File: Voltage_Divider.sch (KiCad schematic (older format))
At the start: 36 parts, among them J24 test, J25 CONN_01X05, J26 test, J27 test, U19 ACPL-W343, U20 ACPL-W343, U21 ANA4522

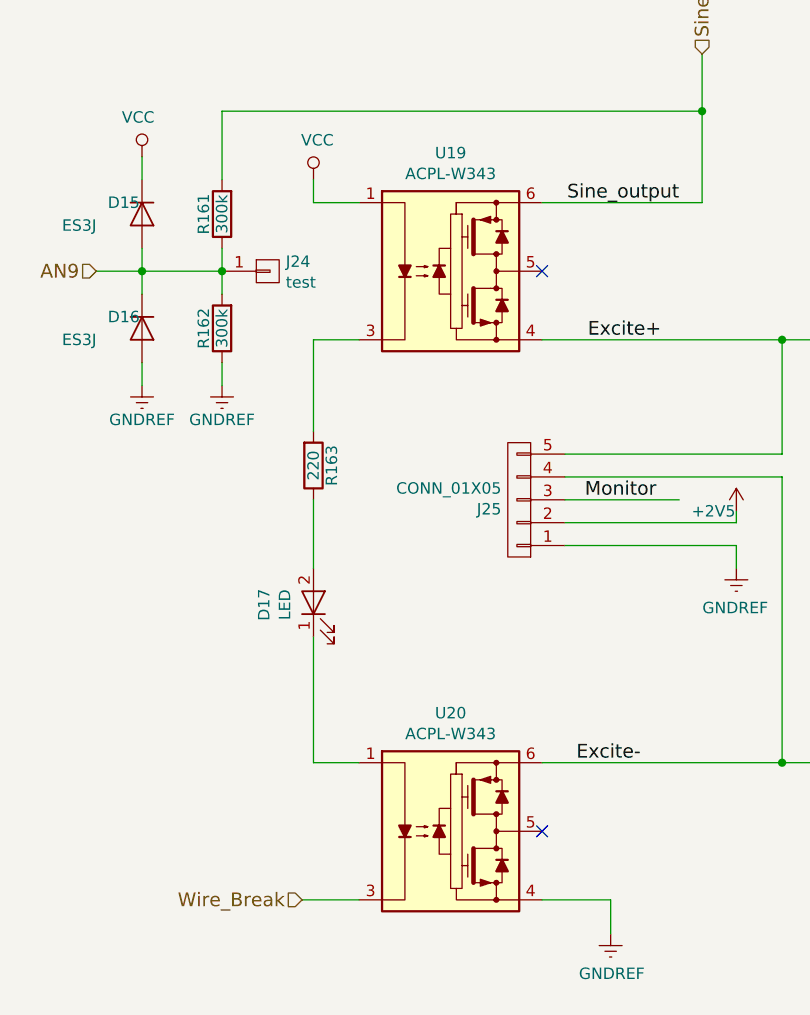
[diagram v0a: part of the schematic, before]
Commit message: 2차 PCB 1차 수정
1. ADR455 Vcc V12 수정
2. DCDC 입력전압 변경
3. Bypass 콘덴서 C66, C67 추가
4. SOIC 방향 표시
5. TLV431 PADS 변경
6. AQV258 Pin3 --> Pin2
7. 전해콘덴서 방향추가
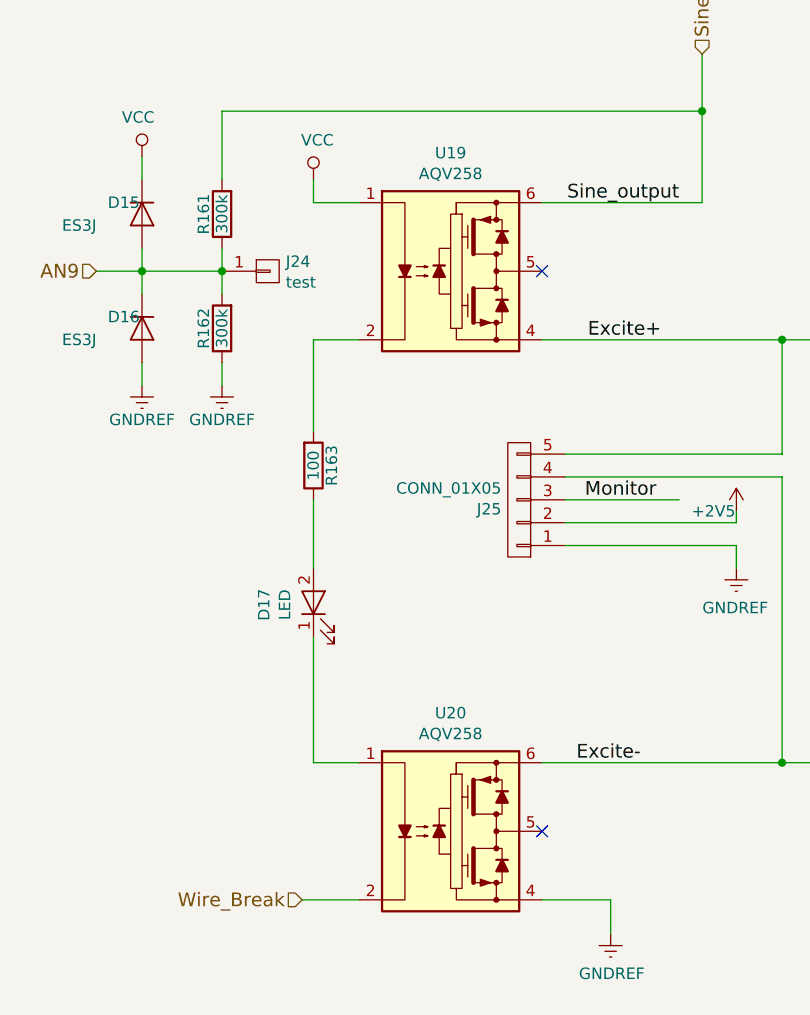
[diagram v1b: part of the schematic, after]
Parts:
- removed U19, U20: ACPL-W343, Housings_DIP:DIP-6_W7.62mm, symbol ACPL-W343
- added U19, U20: AQV258, Housings_DIP:DIP-6_W7.62mm_Socket, symbol AQV258
- R163: value 220 -> 100
- U21: footprint Housings_SOIC:SOIC-8-1EP_3.9x4.9mm_Pitch1.27mm -> USER:SOIC-8_3.9x4.9mm_Pitch1.27mm
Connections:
- net Excite+: now also U19.4 (VEE)
- net Excite-: now also U20.6 (VCC)
- net GNDREF: now also U20.4 (VEE)
- net Sine: now also U19.6 (VCC)
- net VCC: now also U19.1 (A)
- net Wire_Break: now also U20.2 (C)
- net at R163.2: now also U19.2 (C)
- net at D17.1 (K): now also U20.1 (A)
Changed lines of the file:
@@
 F 0 "U21" H 9891 2996 50  0000 L CNN
 F 1 "ANA4522" H 9891 2905 50  0000 L CNN
-F 2 "Housings_SOIC:SOIC-8-1EP_3.9x4.9mm_Pitch1.27mm" H 9550 2950 50  0001 C CNN
+F 2 "USER:SOIC-8_3.9x4.9mm_Pitch1.27mm" H 9550 2950 50  0001 C CNN
 F 3 "" H 9550 2950 50  0001 C CNN
 	1    9550 2950
@@
 P 3500 3400
 F 0 "R163" V 3580 3400 50  0000 C CNN
-F 1 "220" V 3500 3400 50  0000 C CNN
+F 1 "100" V 3500 3400 50  0000 C CNN
 F 2 "Resistors_SMD:R_0805_HandSoldering" V 3430 3400 50  0001 C CNN
 F 3 "" H 3500 3400 50  0001 C CNN
@@
 Text Label 5100 2250 2    60   ~ 0
 Sine_output
-$Comp
-L ACPL-W343 U20
-U 1 1 5B064611
-P 4100 5000
-F 0 "U20" H 4100 5517 50  0000 C CNN
-F 1 "ACPL-W343" H 4100 5426 50  0000 C CNN
-F 2 "Housings_DIP:DIP-6_W7.62mm" H 4100 4600 50  0001 C CIN
-F 3 "" H 4010 5005 50  0001 L CNN
-	1    4100 5000
-	1    0    0    -1
-$EndComp
 NoConn ~ 4500 5000
-$Comp
-L ACPL-W343 U19
-U 1 1 5B06461B
-P 4100 2550
-F 0 "U19" H 4100 3067 50  0000 C CNN
-F 1 "ACPL-W343" H 4100 2976 50  0000 C CNN
-F 2 "Housings_DIP:DIP-6_W7.62mm" H 4100 2150 50  0001 C CIN
-F 3 "" H 4010 2555 50  0001 L CNN
-	1    4100 2550
-	1    0    0    -1
-$EndComp
 $Comp
 L 1N4004 D16
@@
 Wire Wire Line
 	4500 2850 8000 2850
+$Comp
+L AQV258 U19
+U 1 1 5B1E85BB
+P 4100 2550
+F 0 "U19" H 4100 3067 50  0000 C CNN
+F 1 "AQV258" H 4100 2976 50  0000 C CNN
+F 2 "Housings_DIP:DIP-6_W7.62mm_Socket" H 4100 2150 50  0001 C CIN
+F 3 "" H 4010 2555 50  0001 L CNN
+	1    4100 2550
+	1    0    0    -1
+$EndComp
+$Comp
+L AQV258 U20
+U 1 1 5B1E8691
+P 4100 5000
+F 0 "U20" H 4100 5517 50  0000 C CNN
+F 1 "AQV258" H 4100 5426 50  0000 C CNN
+F 2 "Housings_DIP:DIP-6_W7.62mm_Socket" H 4100 4600 50  0001 C CIN
+F 3 "" H 4010 5005 50  0001 L CNN
+	1    4100 5000
+	1    0    0    -1
+$EndComp
 $EndSCHEMATC

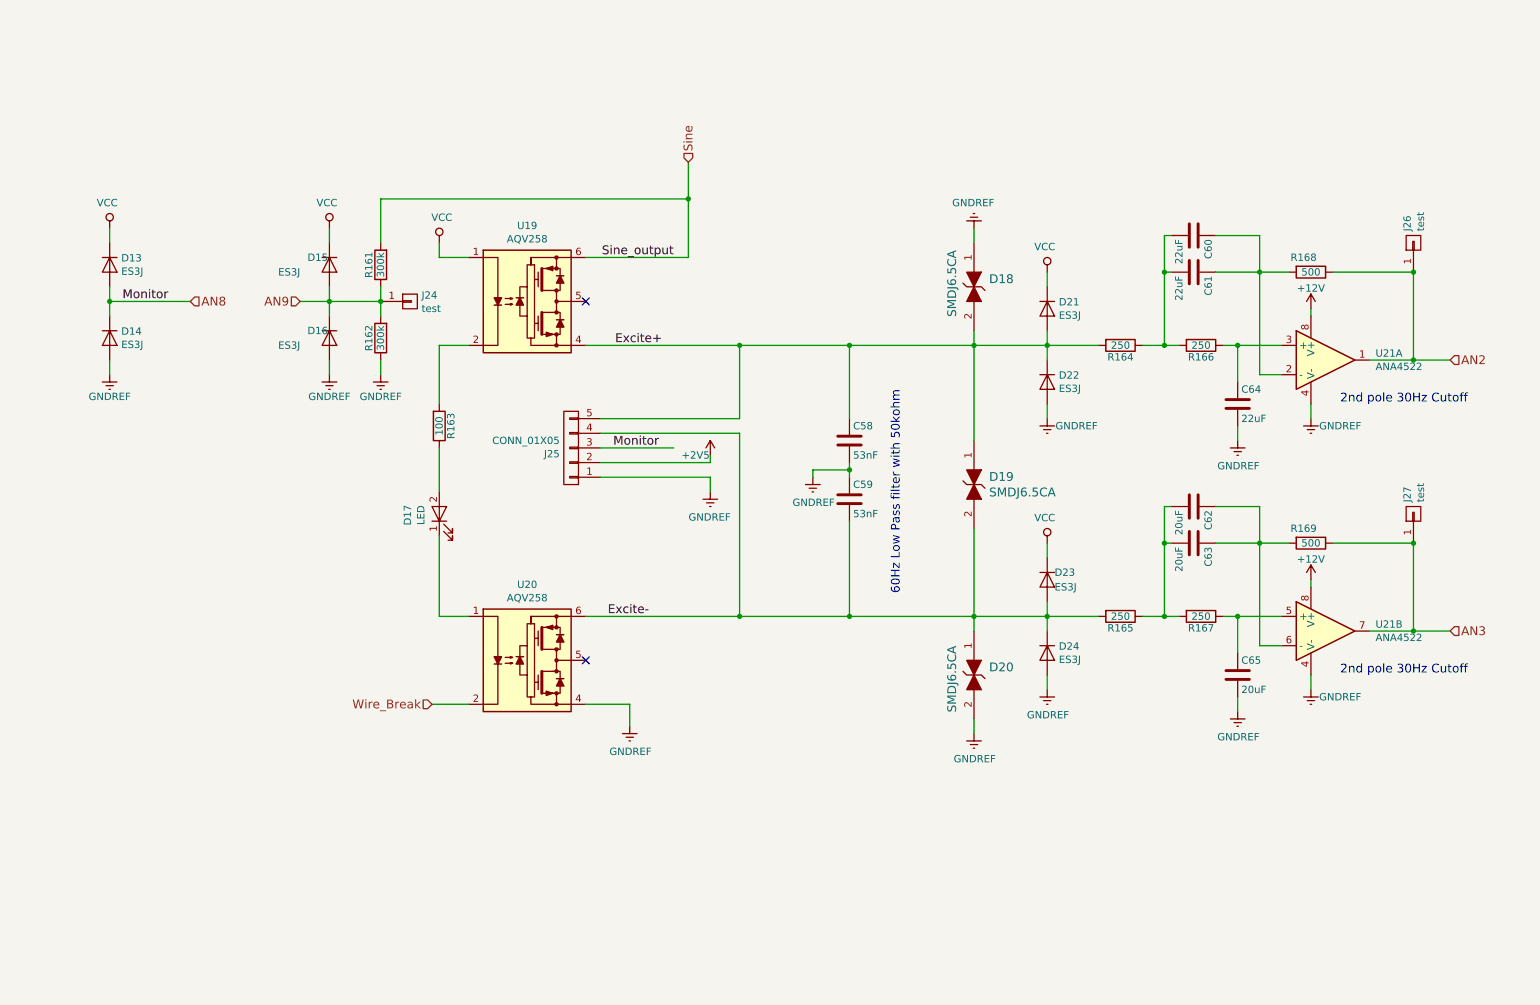
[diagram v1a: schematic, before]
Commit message: 0805_넓히기
기타 수정
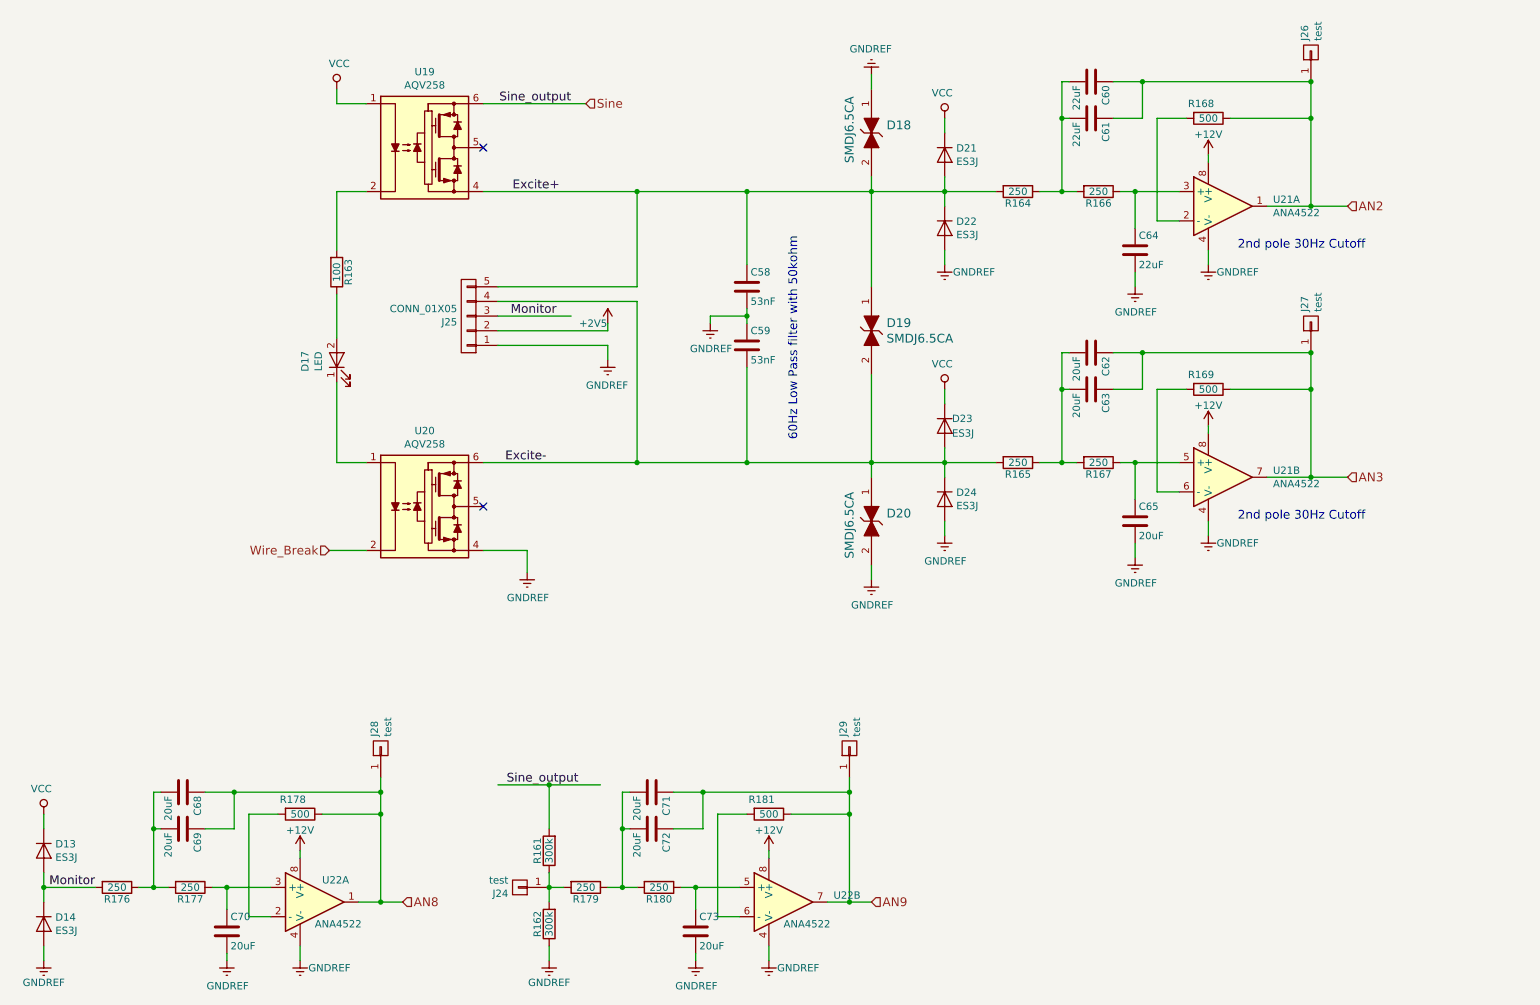
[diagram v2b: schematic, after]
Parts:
- removed D15, D16: ES3J, Diodes_SMD:D_SMC_Handsoldering, symbol 1N4004
- added C68, C69, C70, C71, C72, C73: 20uF, Capacitors_SMD:C_1210_HandSoldering, symbol C
- added J28, J29: test, Pin_Headers:Pin_Header_Straight_1x01_Pitch2.00mm, symbol CONN_01X01
- added R176, R177, R179, R180: 250, Resistors_SMD:R_0805_HandSoldering, symbol R
- added R178, R181: 500, Resistors_SMD:R_0805_HandSoldering, symbol R
- added U22: ANA4522, USER:SOIC-8_3.9x4.9mm_Pitch1.27mm, symbol LM358
- D13, D14, D21, D22, D23, D24: footprint Diodes_SMD:D_SMC_Handsoldering -> USER:D_SMC_Handsoldering
- U21: footprint Housings_SOIC:SOIC-8-1EP_3.9x4.9mm_Pitch1.27mm -> USER:SOIC-8_3.9x4.9mm_Pitch1.27mm
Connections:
- net +12V: now also U22.8 (V+), U22.8 (V+)
- net AN2: now also C60.1, C61.1
- net AN3: now also C62.1, C63.1
- net AN8: now also C68.1, C69.1, J28.1 (P1), R178.1, U22.1; no longer D13.2 (A), D14.1 (K), J25.3 (P3)
- net AN9: now also C71.1, C72.1, J29.1 (P1), R181.1, U22.7; no longer J24.1 (P1), R161.1, R162.2
- net GNDREF: now also C70.2, C73.2, U22.4 (V-), U22.4 (V-)
- net at R168.2, U21.2 (-): no longer C60.1, C61.1
- net at R169.2, U21.6 (-): no longer C62.1, C63.1
- new net: J24.1 (P1), R161.1, R162.2, R179.2
- new net: R178.2, U22.2 (-)
- new net: C70.1, R177.1, U22.3 (+)
- new net: C68.2, C69.2, R176.1, R177.2
- new net: C71.2, C72.2, R179.1, R180.2
- new net: C73.1, R180.1, U22.5 (+)
- new net: R181.2, U22.6 (-)
- new net Monitor: D13.2 (A), D14.1 (K), J25.3 (P3), R176.2
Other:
- moved on the sheet: C58, C59, C60, C61, C62, C63, C64, C65, D13, D14, D17, D18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

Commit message: High Voltage reinforce
고전압 부분 보강
AN2, AN3 두 부분 6.5V limit
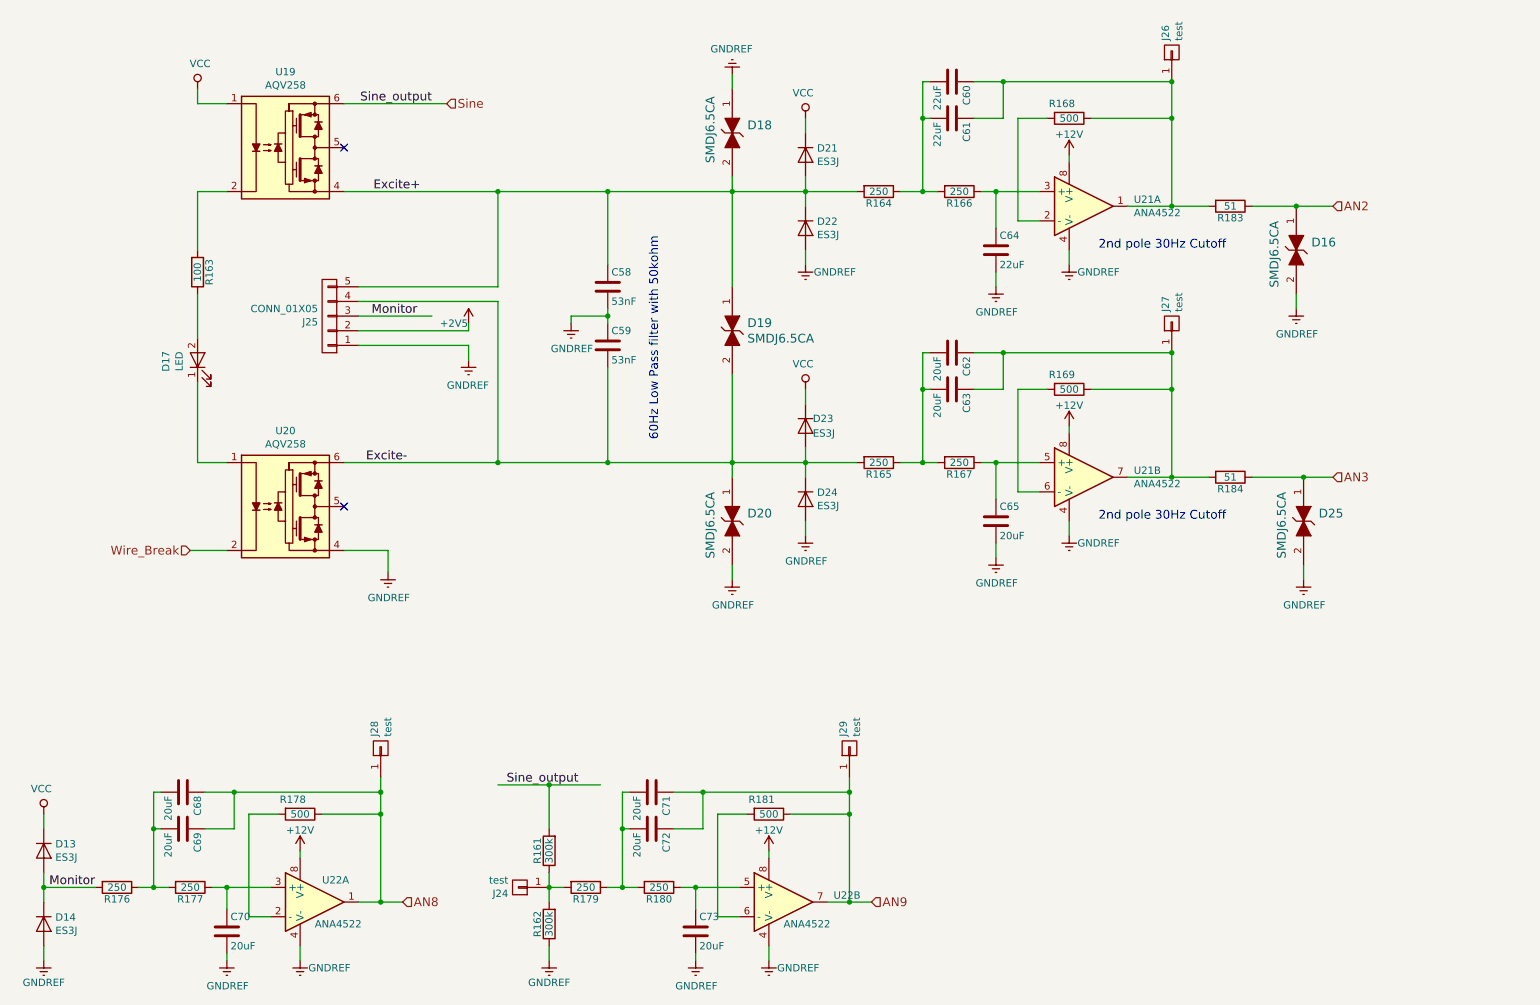
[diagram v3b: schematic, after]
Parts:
- added D16, D25: SMDJ6.5CA, Diodes_SMD:D_SMC_Handsoldering, symbol PGB1010603MR
- added R183, R184: 51, Resistors_SMD:R_0805_HandSoldering, symbol R
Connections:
- net AN2: now also D16.1, R183.1; no longer C60.1, C61.1, J26.1 (P1), R168.1, U21.1
- net AN3: now also D25.1, R184.1; no longer C62.1, C63.1, J27.1 (P1), R169.1, U21.7
- net GNDREF: now also D16.2, D25.2
- new net: C60.1, C61.1, J26.1 (P1), R168.1, R183.2, U21.1
- new net: C62.1, C63.1, J27.1 (P1), R169.1, R184.2, U21.7
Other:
- moved on the sheet: C58, C59, C60, C61, C62, C63, C64, C65, D17, D18, D19, D20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

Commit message: 3차 PCB
1. 모니터 고압부 150k옴 2갤로 수정
2. 6.5V Zener 추가
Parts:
- D18, D19, D20: value SMDJ6.5CA -> SMDJ10
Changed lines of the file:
@@
 P 5500 1400
 F 0 "D18" V 5447 1503 60  0000 L CNN
-F 1 "SMDJ6.5CA" H 5250 1250 60  0000 L CNN
+F 1 "SMDJ10" H 5250 1250 60  0000 L CNN
 F 2 "Diodes_SMD:D_SMC_Handsoldering" H 5700 1600 60  0001 L CNN
 F 3 "http://www.littelfuse.com/data/en/data_sheets/littelfuse_pulseguard-esd_pgb1.pdf" H 5700 1700 60  0001 L CNN
@@
 P 5500 4050
 F 0 "D20" V 5447 4153 60  0000 L CNN
-F 1 "SMDJ6.5CA" H 5300 3900 60  0000 L CNN
+F 1 "SMDJ10" H 5300 3900 60  0000 L CNN
 F 2 "Diodes_SMD:D_SMC_Handsoldering" H 5700 4250 60  0001 L CNN
 F 3 "http://www.littelfuse.com/data/en/data_sheets/littelfuse_pulseguard-esd_pgb1.pdf" H 5700 4350 60  0001 L CNN
@@
 P 5500 2750
 F 0 "D19" V 5447 2853 60  0000 L CNN
-F 1 "SMDJ6.5CA" V 5553 2853 60  0000 L CNN
+F 1 "SMDJ10" V 5553 2853 60  0000 L CNN
 F 2 "Diodes_SMD:D_SMC_Handsoldering" H 5700 2950 60  0001 L CNN
 F 3 "http://www.littelfuse.com/data/en/data_sheets/littelfuse_pulseguard-esd_pgb1.pdf" H 5700 3050 60  0001 L CNN
